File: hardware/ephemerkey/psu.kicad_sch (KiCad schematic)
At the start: 21 parts, among them J3 USB-C, J4 BAT 1S Li-ion, Q1 AO3401A, U2 TPS63900DSKR, U3 USBLC6-2SC6, U4 MCP73831-2-OT

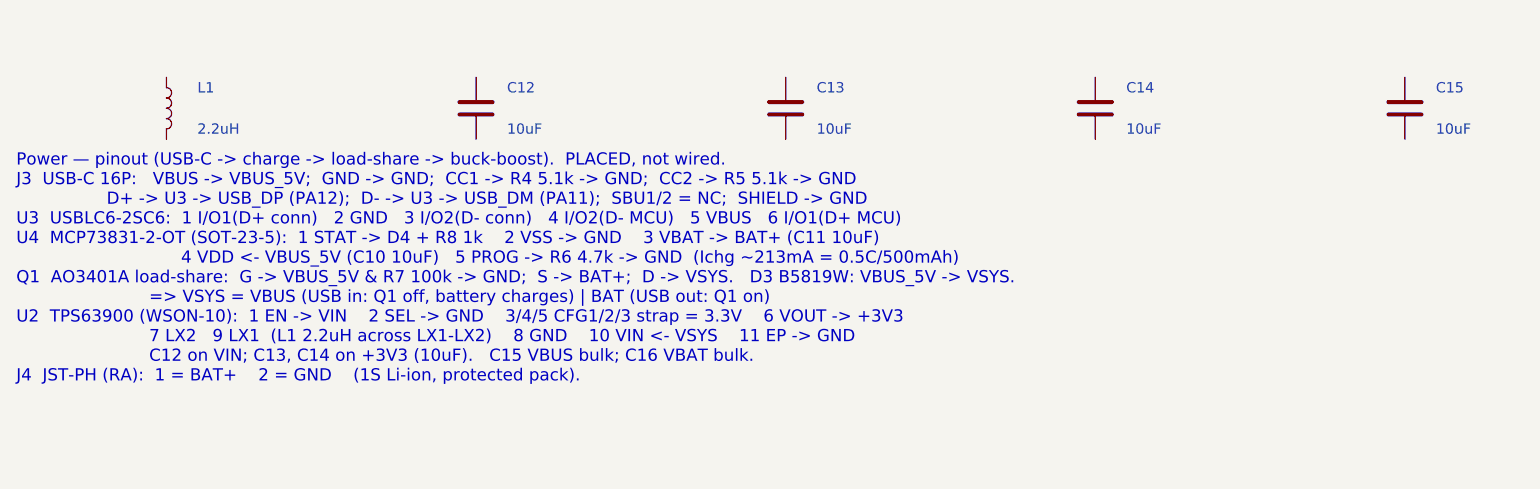
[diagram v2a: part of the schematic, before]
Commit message: lock: second servo output, clearer wiring notes, start PCB layout
- Add a second servo output (J8 + SERVO_SIG2 on PB4, R24/R25) sharing the
  VSERVO rail and the load-switch/interlock -- e.g. a dual-latch lock.
- Rewrite the per-sheet wiring notes (MCU/PWR/DRV) from prose into terse
  pin -> net maps: one line per part, every pin = its net, with a NETS IN
  header for cross-sheet signals. Rationale stays in the README.
- kschgen: park the wiring note below all placed components so the text no
  longer overlaps symbols (computed from the last component row).
- Start the lock PCB layout (hardware/lock/lock.kicad_pcb).

Board regenerates + checks clean (49 components; all footprints carry 3D models).

Co-Authored-By: Claude Opus 4.8 (1M context) <noreply@anthropic.com>
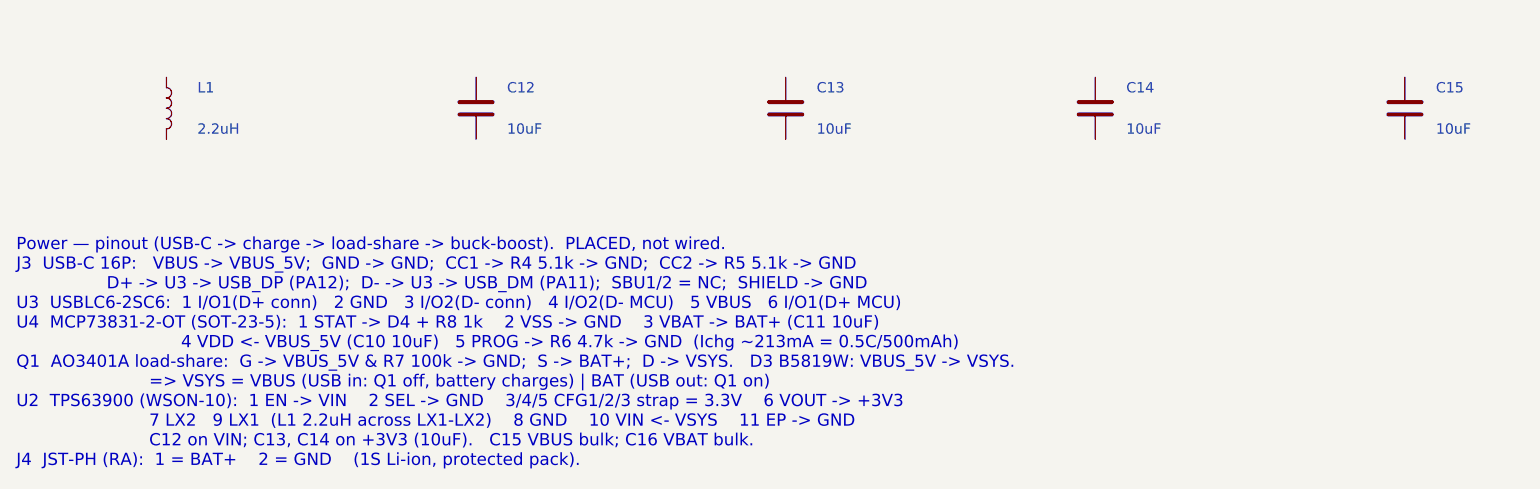
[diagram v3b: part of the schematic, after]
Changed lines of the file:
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@@
 		(instances
 			(project "ephemerkey"
-				(path "/e1000000-0000-4000-8000-000000000001/946d21ce-bf52-4182-809a-bfd4793f83fe"
+				(path "/e1000000-0000-4000-8000-000000000001/bcb4810a-549d-47ce-b8ca-ab8890e1d103"
 					(reference "J3")
 					(unit 1)
@@
 		(instances
 			(project "ephemerkey"
-				(path "/e1000000-0000-4000-8000-000000000001/946d21ce-bf52-4182-809a-bfd4793f83fe"
+				(path "/e1000000-0000-4000-8000-000000000001/bcb4810a-549d-47ce-b8ca-ab8890e1d103"
 					(reference "J4")
 					(unit 1)
@@
 		(instances
 			(project "ephemerkey"
-				(path "/e1000000-0000-4000-8000-000000000001/946d21ce-bf52-4182-809a-bfd4793f83fe"
+				(path "/e1000000-0000-4000-8000-000000000001/bcb4810a-549d-47ce-b8ca-ab8890e1d103"
 					(reference "U2")
 					(unit 1)
@@
 		(instances
 			(project "ephemerkey"
-				(path "/e1000000-0000-4000-8000-000000000001/946d21ce-bf52-4182-809a-bfd4793f83fe"
+				(path "/e1000000-0000-4000-8000-000000000001/bcb4810a-549d-47ce-b8ca-ab8890e1d103"
 					(reference "U3")
 					(unit 1)
@@
 		(instances
 			(project "ephemerkey"
-				(path "/e1000000-0000-4000-8000-000000000001/946d21ce-bf52-4182-809a-bfd4793f83fe"
+				(path "/e1000000-0000-4000-8000-000000000001/bcb4810a-549d-47ce-b8ca-ab8890e1d103"
 					(reference "R4")
 					(unit 1)
@@
 		(instances
 			(project "ephemerkey"
-				(path "/e1000000-0000-4000-8000-000000000001/946d21ce-bf52-4182-809a-bfd4793f83fe"
+				(path "/e1000000-0000-4000-8000-000000000001/bcb4810a-549d-47ce-b8ca-ab8890e1d103"
 					(reference "R5")
 					(unit 1)
@@
 		(instances
 			(project "ephemerkey"
-				(path "/e1000000-0000-4000-8000-000000000001/946d21ce-bf52-4182-809a-bfd4793f83fe"
+				(path "/e1000000-0000-4000-8000-000000000001/bcb4810a-549d-47ce-b8ca-ab8890e1d103"
 					(reference "U4")
 					(unit 1)
@@
 		(instances
 			(project "ephemerkey"
-				(path "/e1000000-0000-4000-8000-000000000001/946d21ce-bf52-4182-809a-bfd4793f83fe"
+				(path "/e1000000-0000-4000-8000-000000000001/bcb4810a-549d-47ce-b8ca-ab8890e1d103"
 					(reference "R6")
 					(unit 1)
@@
 		(instances
 			(project "ephemerkey"
-				(path "/e1000000-0000-4000-8000-000000000001/946d21ce-bf52-4182-809a-bfd4793f83fe"
+				(path "/e1000000-0000-4000-8000-000000000001/bcb4810a-549d-47ce-b8ca-ab8890e1d103"
 					(reference "C10")
 					(unit 1)
@@
 		(instances
 			(project "ephemerkey"
-				(path "/e1000000-0000-4000-8000-000000000001/946d21ce-bf52-4182-809a-bfd4793f83fe"
+				(path "/e1000000-0000-4000-8000-000000000001/bcb4810a-549d-47ce-b8ca-ab8890e1d103"
 					(reference "C11")
 					(unit 1)
@@
 		(instances
 			(project "ephemerkey"
-				(path "/e1000000-0000-4000-8000-000000000001/946d21ce-bf52-4182-809a-bfd4793f83fe"
+				(path "/e1000000-0000-4000-8000-000000000001/bcb4810a-549d-47ce-b8ca-ab8890e1d103"
 					(reference "Q1")
 					(unit 1)
@@
 		(instances
 			(project "ephemerkey"
-				(path "/e1000000-0000-4000-8000-000000000001/946d21ce-bf52-4182-809a-bfd4793f83fe"
+				(path "/e1000000-0000-4000-8000-000000000001/bcb4810a-549d-47ce-b8ca-ab8890e1d103"
 					(reference "D3")
 					(unit 1)
@@
 		(instances
 			(project "ephemerkey"
-				(path "/e1000000-0000-4000-8000-000000000001/946d21ce-bf52-4182-809a-bfd4793f83fe"
+				(path "/e1000000-0000-4000-8000-000000000001/bcb4810a-549d-47ce-b8ca-ab8890e1d103"
 					(reference "R7")
 					(unit 1)
@@
 		(instances
 			(project "ephemerkey"
-				(path "/e1000000-0000-4000-8000-000000000001/946d21ce-bf52-4182-809a-bfd4793f83fe"
+				(path "/e1000000-0000-4000-8000-000000000001/bcb4810a-549d-47ce-b8ca-ab8890e1d103"
 					(reference "L1")
 					(unit 1)
@@
 		(instances
 			(project "ephemerkey"
-				(path "/e1000000-0000-4000-8000-000000000001/946d21ce-bf52-4182-809a-bfd4793f83fe"
+				(path "/e1000000-0000-4000-8000-000000000001/bcb4810a-549d-47ce-b8ca-ab8890e1d103"
 					(reference "C12")
 					(unit 1)
@@
 		(instances
 			(project "ephemerkey"
-				(path "/e1000000-0000-4000-8000-000000000001/946d21ce-bf52-4182-809a-bfd4793f83fe"
+				(path "/e1000000-0000-4000-8000-000000000001/bcb4810a-549d-47ce-b8ca-ab8890e1d103"
 					(reference "C13")
 					(unit 1)
@@
 		(instances
 			(project "ephemerkey"
-				(path "/e1000000-0000-4000-8000-000000000001/946d21ce-bf52-4182-809a-bfd4793f83fe"
+				(path "/e1000000-0000-4000-8000-000000000001/bcb4810a-549d-47ce-b8ca-ab8890e1d103"
 					(reference "C14")
 					(unit 1)
@@
 		(instances
 			(project "ephemerkey"
-				(path "/e1000000-0000-4000-8000-000000000001/946d21ce-bf52-4182-809a-bfd4793f83fe"
+				(path "/e1000000-0000-4000-8000-000000000001/bcb4810a-549d-47ce-b8ca-ab8890e1d103"
 					(reference "C15")
 					(unit 1)
@@
 		(instances
 			(project "ephemerkey"
-				(path "/e1000000-0000-4000-8000-000000000001/946d21ce-bf52-4182-809a-bfd4793f83fe"
+				(path "/e1000000-0000-4000-8000-000000000001/bcb4810a-549d-47ce-b8ca-ab8890e1d103"
 					(reference "C16")
 					(unit 1)
@@
 		(instances
 			(project "ephemerkey"
-				(path "/e1000000-0000-4000-8000-000000000001/946d21ce-bf52-4182-809a-bfd4793f83fe"
+				(path "/e1000000-0000-4000-8000-000000000001/bcb4810a-549d-47ce-b8ca-ab8890e1d103"
 					(reference "D4")
 					(unit 1)
@@
 		(instances
 			(project "ephemerkey"
-				(path "/e1000000-0000-4000-8000-000000000001/946d21ce-bf52-4182-809a-bfd4793f83fe"
+				(path "/e1000000-0000-4000-8000-000000000001/bcb4810a-549d-47ce-b8ca-ab8890e1d103"
 					(reference "R8")
 					(unit 1)
@@
 	(text "Power — pinout (USB-C -> charge -> load-share -> buck-boost).  PLACED, not wired.\nJ3  USB-C 16P:   VBUS -> VBUS_5V;  GND -> GND;  CC1 -> R4 5.1k -> GND;  CC2 -> R5 5.1k -> GND\n                 D+ -> U3 -> USB_DP (PA12);  D- -> U3 -> USB_DM (PA11);  SBU1/2 = NC;  SHIELD -> GND\nU3  USBLC6-2SC6:  1 I/O1(D+ conn)   2 GND   3 I/O2(D- conn)   4 I/O2(D- MCU)   5 VBUS   6 I/O1(D+ MCU)\nU4  MCP73831-2-OT (SOT-23-5):  1 STAT -> D4 + R8 1k    2 VSS -> GND    3 VBAT -> BAT+ (C11 10uF)\n                               4 VDD <- VBUS_5V (C10 10uF)   5 PROG -> R6 4.7k -> GND  (Ichg ~213mA = 0.5C/500mAh)\nQ1  AO3401A load-share:  G -> VBUS_5V & R7 100k -> GND;  S -> BAT+;  D -> VSYS.   D3 B5819W: VBUS_5V -> VSYS.\n                         => VSYS = VBUS (USB in: Q1 off, battery charges) | BAT (USB out: Q1 on)\nU2  TPS63900 (WSON-10):  1 EN -> VIN    2 SEL -> GND    3/4/5 CFG1/2/3 strap = 3.3V    6 VOUT -> +3V3\n                         7 LX2   9 LX1  (L1 2.2uH across LX1-LX2)    8 GND    10 VIN <- VSYS    11 EP -> GND\n                         C12 on VIN; C13, C14 on +3V3 (10uF).   C15 VBUS bulk; C16 VBAT bulk.\nJ4  JST-PH (RA):  1 = BAT+    2 = GND    (1S Li-ion, protected pack)."
 		(exclude_from_sim no)
-		(at 12.00 158.00 0)
+		(at 12.00 168.40 0)
 		(effects (font (size 1.5 1.5)) (justify left top))
 	)

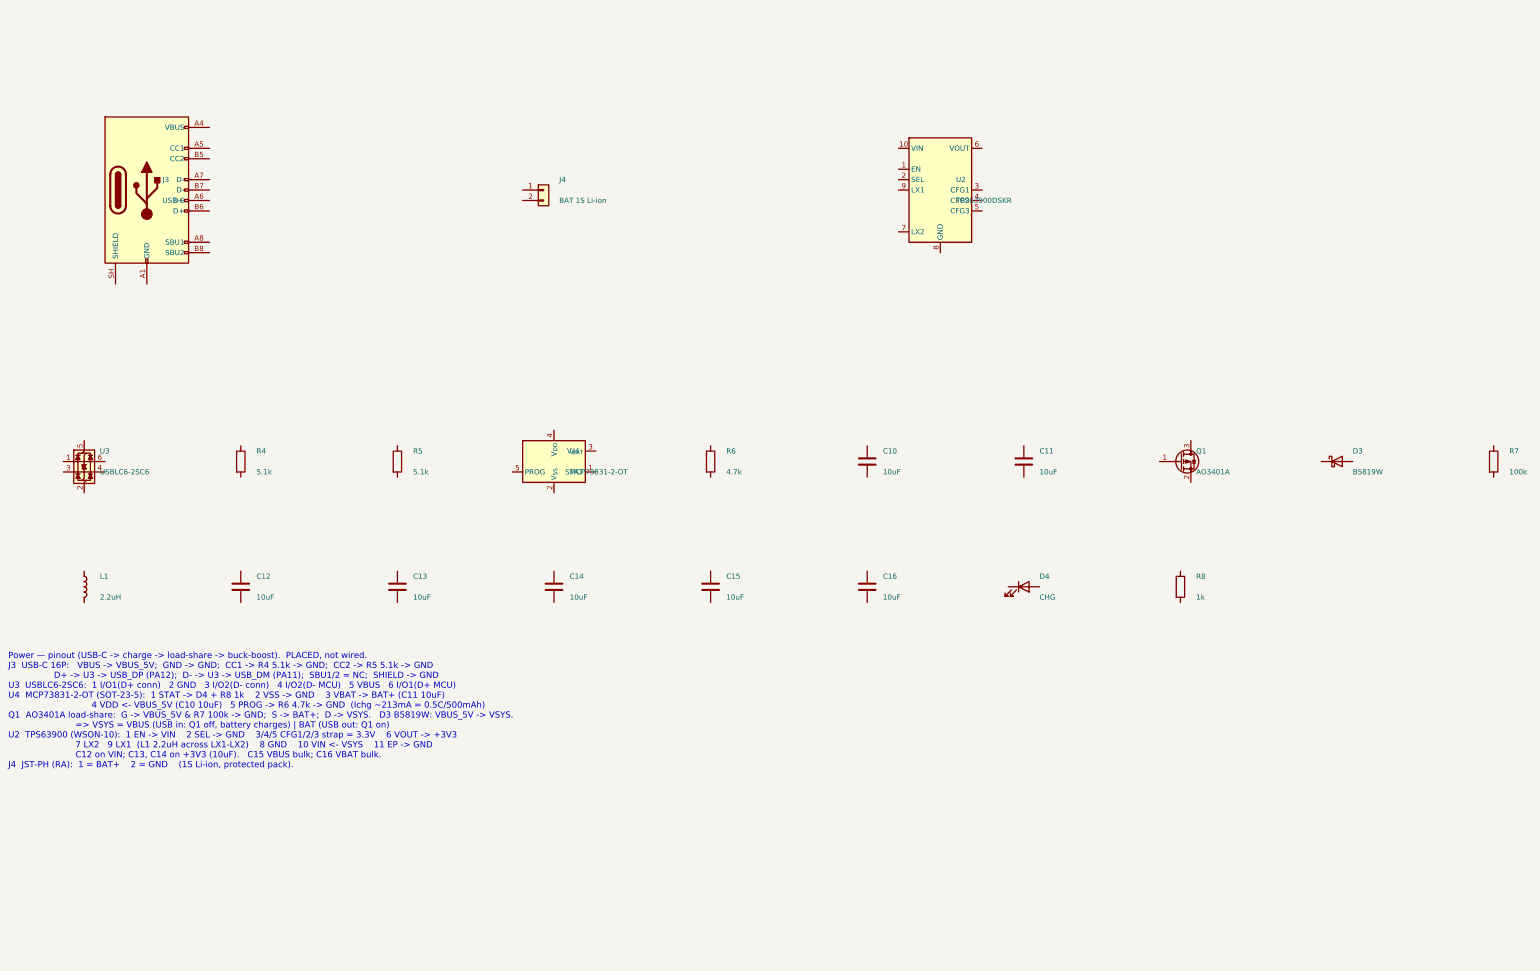
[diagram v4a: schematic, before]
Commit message: ephemerkey: add buzzer (PB4/TIM3_CH1), 2nd vertical USB-C, antenna 1.8pF shunt
- Beeper: LS1 MLT-8530 (C94599, 3.6V magnetic transducer) + AO3400A low-side
  driver (Q2) + 1N4148W flyback (D5) + gate 100R/100k, driven by PB4/TIM3_CH1.
  PB4 verified as TIM3_CH1 (AF1) on the U0 family AF map; TIM3 free (PPS uses TIM2).
  Buzzer footprint is the CUI CMT-8504 placeholder -- verify vs MLT-8530 at layout.
- 2nd USB-C: J5 GCT USB4085 (C7095263), vertical, same 16-pin USB2.0 family,
  same bus as J3 (parallel VBUS/D+/D-/GND) with its own CC pulldowns R15/R16.
- Antenna: populate Cm2 = 1.8pF shunt (W3011A datasheet reference value; the -A's
  rated -16dB is measured with shunt 1.8pF), Cm3 DNP; VNA-trim at bring-up.
  MAX-M10S RF_IN has internal DC block -> no external DC-block cap. Refs: Pulse
  W3011A datasheet + u-blox MAX-M10S integration manual UBX-20053088.

Regenerated (70 components, all footprints assigned + 3D models). DESIGN.md +
per-sheet notes updated. ephemerkey was placed-not-wired, so no wiring lost.

Co-Authored-By: Claude Opus 4.8 (1M context) <noreply@anthropic.com>
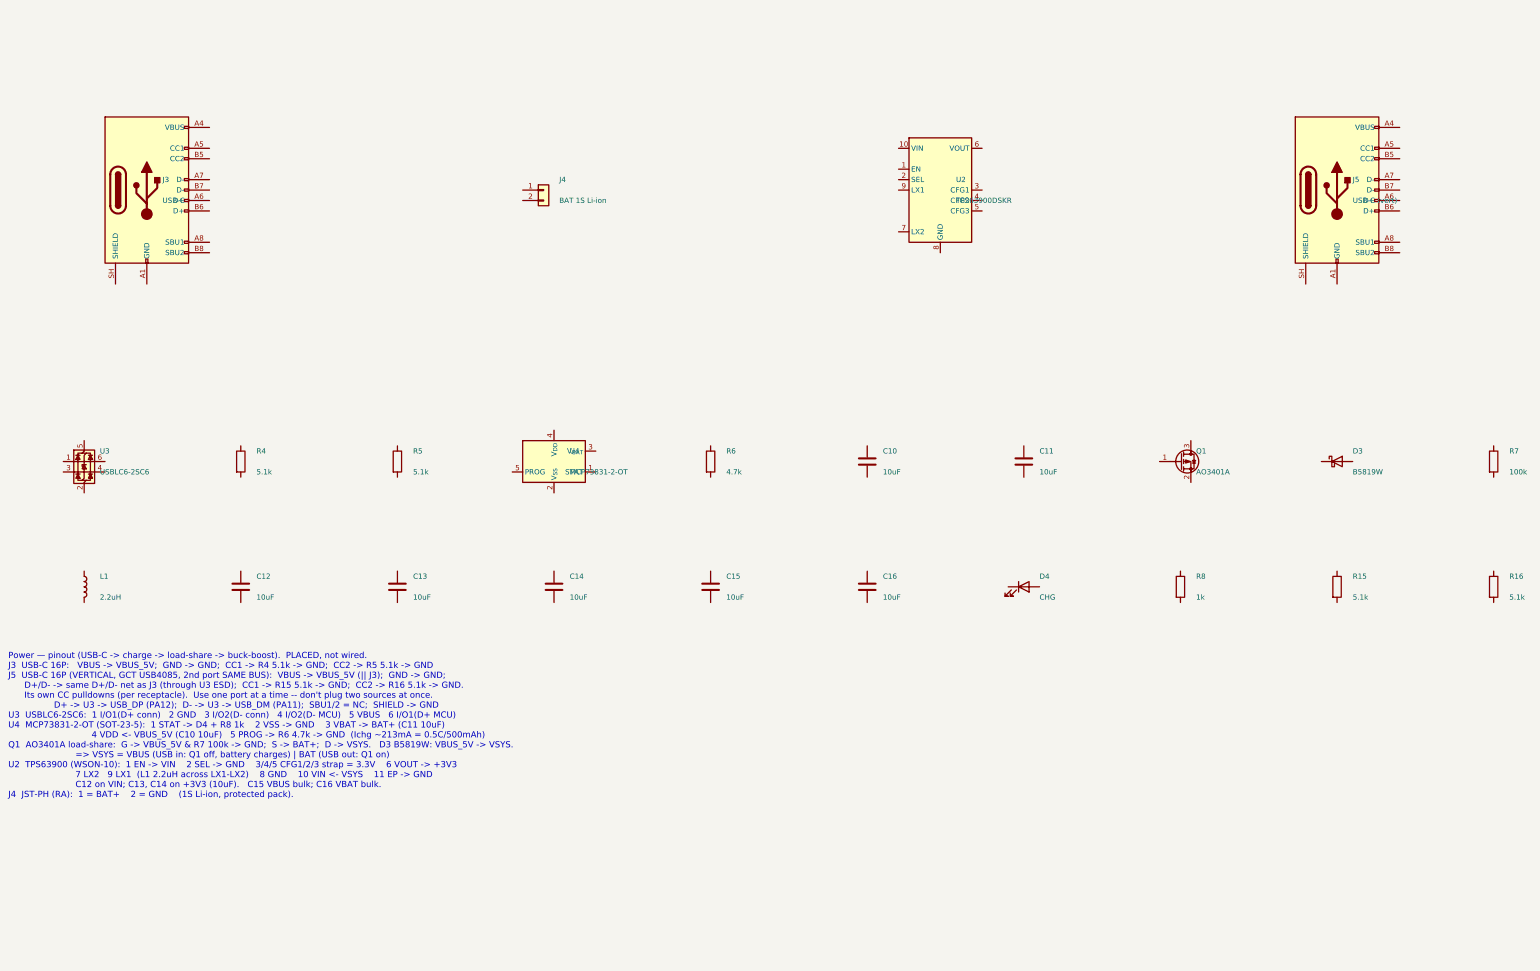
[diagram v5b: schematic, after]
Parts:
- added J5: USB-C (vert), Connector_USB:USB_C_Receptacle_GCT_USB4085, symbol Connector:USB_C_Receptacle_USB2.0_16P
- added R15, R16: 5.1k, Resistor_SMD:R_0402_1005Metric, symbol Device:R
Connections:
- new net: J5.A1 (GND), J5.A12 (GND), J5.B1 (GND), J5.B12 (GND)
- new net: J5.A4 (VBUS), J5.A9 (VBUS), J5.B4 (VBUS), J5.B9 (VBUS)
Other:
- note added: "Power — pinout (USB-C -> charge -> load-share -> buck-boost). PLACED, not wired. J3 USB-C 16P: VBUS -> VBUS_5V; GND -> GND; CC1 -> R4 5.1k -> GND; CC2 -> R5 5.1k -> GND J5 USB-C 16P (VERTICAL, GCT USB4085, 2nd port SAME BUS): VBUS -> VBUS_5V (|| J3); GND -> GND; D+/D- -> same D+/D- net as J3 (through U3 ESD); CC1 -> R15 5.1k -> GND; CC2 -> R16 5.1k -> GND. Its own CC pulldowns (per receptacle). U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"
- note removed: "Power — pinout (USB-C -> charge -> load-share -> buck-boost). PLACED, not wired. J3 USB-C 16P: VBUS -> VBUS_5V; GND -> GND; CC1 -> R4 5.1k -> GND; CC2 -> R5 5.1k -> GND D+ -> U3 -> USB_DP (PA12); D- -> U3 -> USB_DM (PA11); SBU1/2 = NC; SHIELD -> GND U3 USBLC6-2SC6: 1 I/O1(D+ conn) 2 GND 3 I/O2(D- conn) 4 I/O2(D- MCU) 5 VBUS 6 I/O1(D+ MCU) U4 MCP73831-2-OT (SOT-23-5): 1 STAT -> D4 + R8 1k 2 VSS ->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"
